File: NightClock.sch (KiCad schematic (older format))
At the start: 11 parts, among them SW1 PUSH+, SW2 PUSHOK, SW3 PUSH-

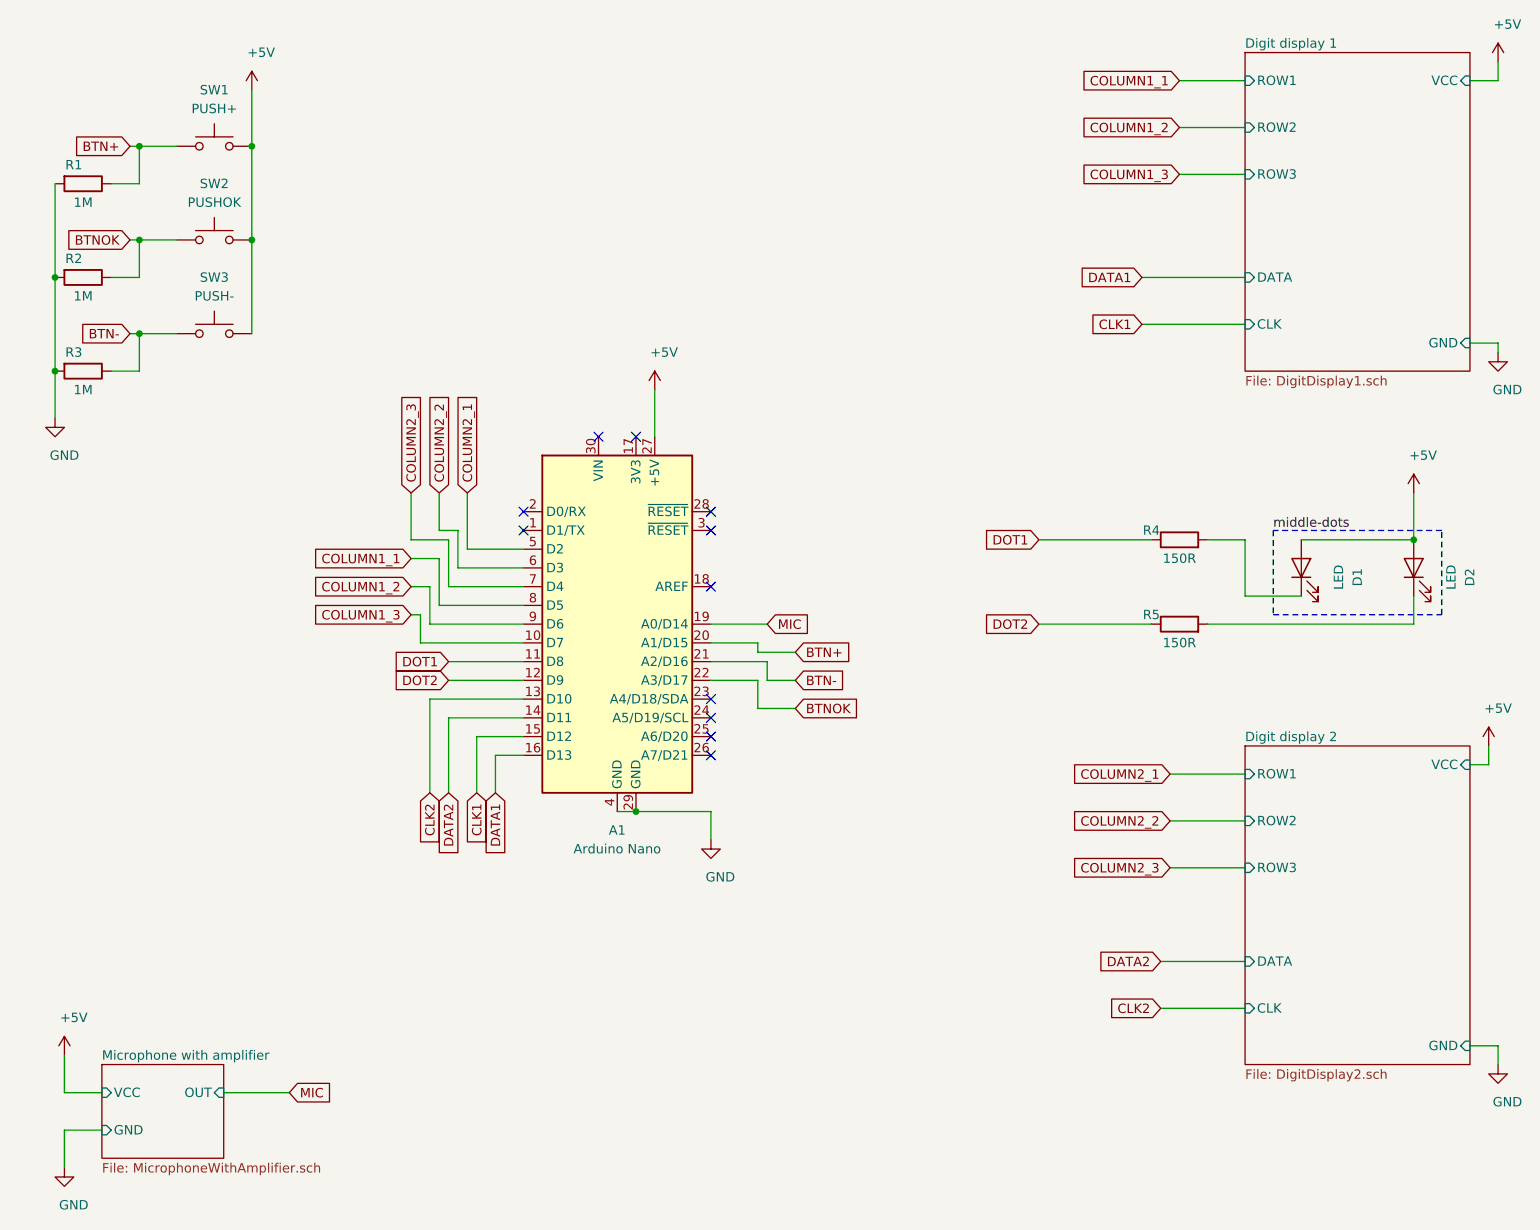
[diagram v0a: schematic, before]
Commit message: add a comparator for setting up an interrupt
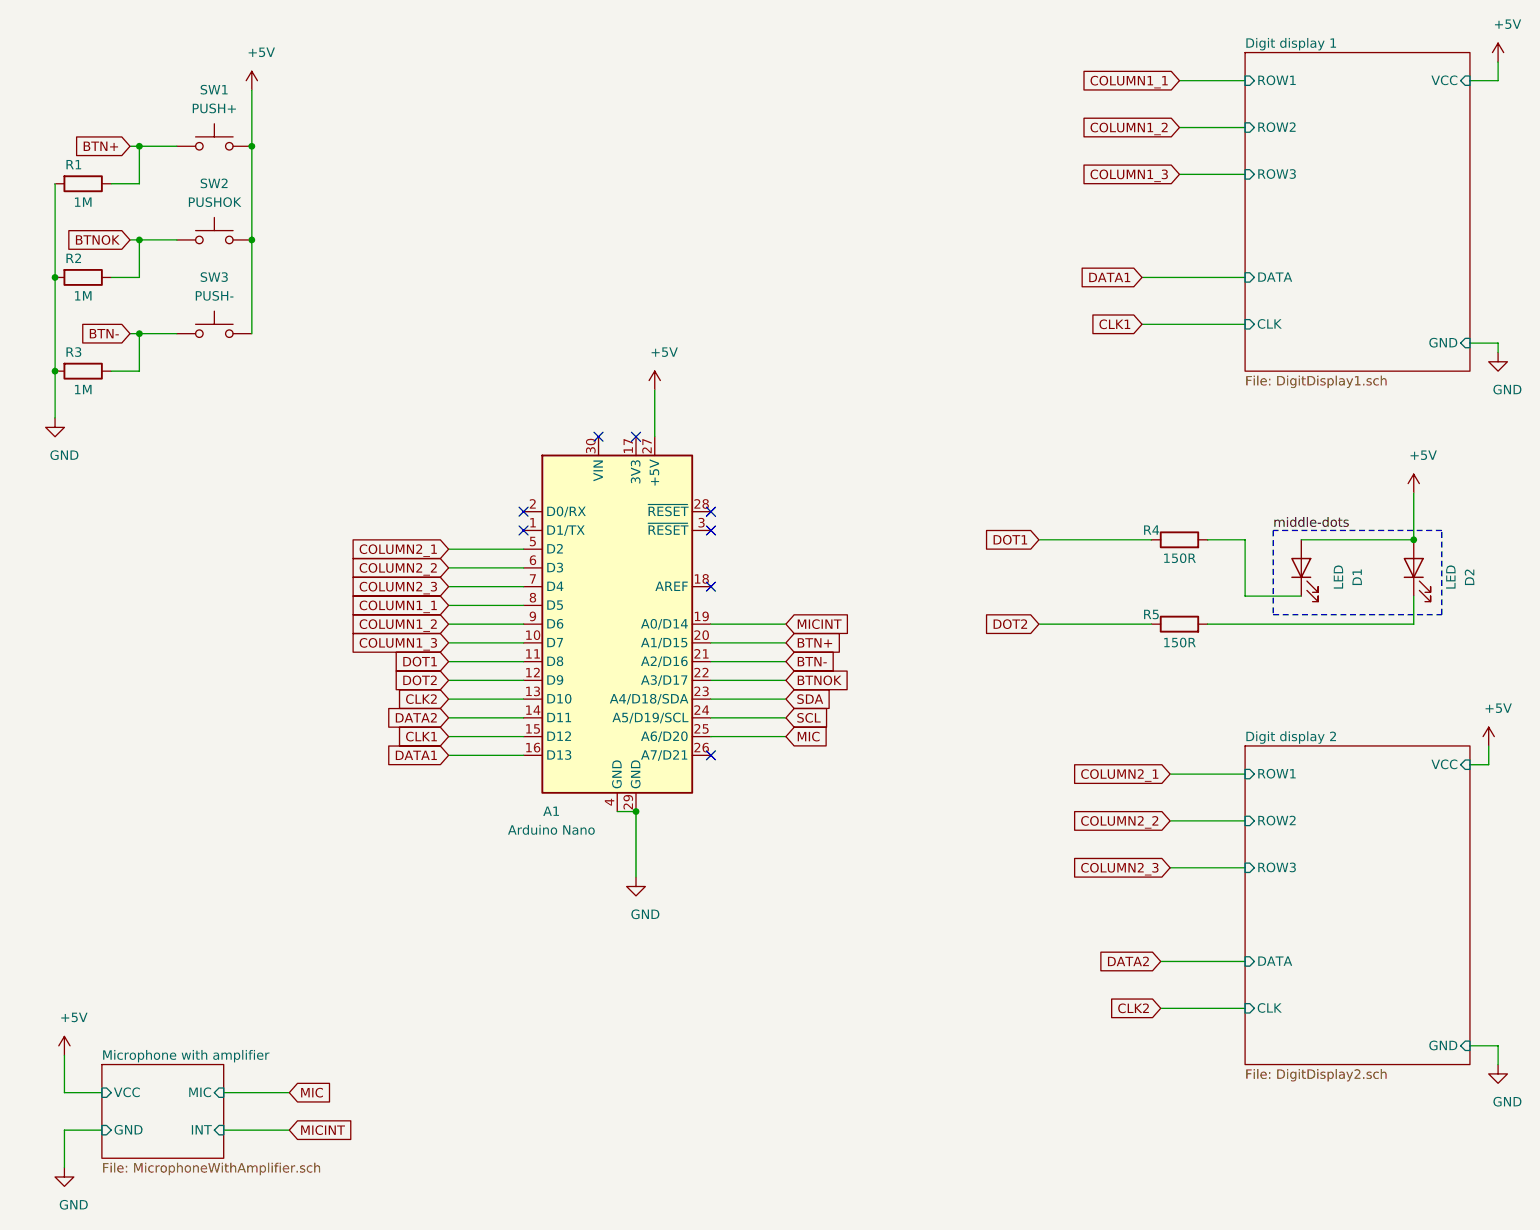
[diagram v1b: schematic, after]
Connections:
- net MIC: now also A1.25 (A6/D20); no longer A1.19 (A0/D14)
- net SDA: now reaches A1.23 (A4/D18/SDA)
- net SCL: now reaches A1.24 (A5/D19/SCL)
- new net MICINT: A1.19 (A0/D14)
- no-connect marks 11 -> 8
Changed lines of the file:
@@
 Sheet 1 4
 Title "Night clock"
-Date "2020-04-10"
+Date "2020-04-11"
 Rev "1"
 Comp "Džejky"
@@
 U 1 1 5E8101CD
 P 4150 3800
-F 0 "A1" H 4150 2700 50  0000 C CNN
-F 1 "Arduino Nano" H 4150 2600 50  0000 C CNN
+F 0 "A1" H 3800 2800 50  0000 C CNN
+F 1 "Arduino Nano" H 3800 2700 50  0000 C CNN
 F 2 "Module:Arduino_Nano" H 4150 3800 50  0001 C CIN
-F 3 "http://www.mouser.com/pdfdocs/Gravitech_Arduino_Nano3_0.pdf" H 4150 3800 50  0001 C CNN
+F 3 "https://content.arduino.cc/assets/Pinout-NANO_latest.pdf" H 4150 3800 50  0001 C CNN
 	1    4150 3800
 	1    0    0    -1
@@
 L power:GND #PWR06
 U 1 1 5E87F331
-P 4650 4950
-F 0 "#PWR06" H 4650 4700 50  0001 C CNN
-F 1 "GND" H 4700 4750 50  0000 C CNN
-F 2 "" H 4650 4950 50  0001 C CNN
-F 3 "" H 4650 4950 50  0001 C CNN
-	1    4650 4950
-	1    0    0    -1
-$EndComp
-Wire Wire Line
-	4650 4950 4650 4800
-Wire Wire Line
-	4650 4800 4250 4800
+P 4250 5150
+F 0 "#PWR06" H 4250 4900 50  0001 C CNN
+F 1 "GND" H 4300 4950 50  0000 C CNN
+F 2 "" H 4250 5150 50  0001 C CNN
+F 3 "" H 4250 5150 50  0001 C CNN
+	1    4250 5150
+	1    0    0    -1
+$EndComp
+Wire Wire Line
+	4250 5150 4250 4800
 Connection ~ 4250 4800
 Wire Wire Line
@@
 Text GLabel 2400 6300 2    50   Input ~ 0
 MIC
-Text GLabel 4950 3800 2    50   Input ~ 0
-MIC
-Wire Wire Line
-	4950 3800 4650 3800
-Text GLabel 5100 3950 2    50   Input ~ 0
+Text GLabel 5050 3900 2    50   Input ~ 0
 BTN+
-Text GLabel 5100 4100 2    50   Input ~ 0
+Text GLabel 5050 4000 2    50   Input ~ 0
 BTN-
-Text GLabel 5100 4250 2    50   Input ~ 0
+Text GLabel 5050 4100 2    50   Input ~ 0
 BTNOK
-Wire Wire Line
-	5100 3950 4900 3950
-Wire Wire Line
-	4900 3950 4900 3900
-Wire Wire Line
-	4900 3900 4650 3900
-Wire Wire Line
-	4650 4000 4950 4000
-Wire Wire Line
-	4950 4000 4950 4100
-Wire Wire Line
-	4950 4100 5100 4100
-Wire Wire Line
-	5100 4250 4900 4250
-Wire Wire Line
-	4900 4250 4900 4100
-Wire Wire Line
-	4900 4100 4650 4100
 Text GLabel 1550 1250 0    50   Input ~ 0
 BTN+
@@
 Text GLabel 7050 5850 0    50   Input ~ 0
 CLK2
-Text GLabel 3500 4700 3    50   Input ~ 0
-DATA1
-Text GLabel 3400 4700 3    50   Input ~ 0
-CLK1
-Text GLabel 3250 4700 3    50   Input ~ 0
+Text GLabel 3250 4300 0    50   Input ~ 0
 DATA2
-Text GLabel 3150 4700 3    50   Input ~ 0
+Text GLabel 3250 4200 0    50   Input ~ 0
 CLK2
-Wire Wire Line
-	3500 4700 3500 4500
-Wire Wire Line
-	3500 4500 3650 4500
-Wire Wire Line
-	3650 4400 3400 4400
-Wire Wire Line
-	3400 4400 3400 4700
-Wire Wire Line
-	3650 4300 3250 4300
-Wire Wire Line
-	3250 4300 3250 4700
-Wire Wire Line
-	3650 4200 3150 4200
-Wire Wire Line
-	3150 4200 3150 4700
 Text GLabel 6400 3350 0    50   Input ~ 0
 DOT1
@@
 Wire Wire Line
 	3650 4100 3250 4100
-Text GLabel 3050 3450 0    50   Input ~ 0
+Text GLabel 3250 3700 0    50   Input ~ 0
 COLUMN1_1
-Text GLabel 3050 3600 0    50   Input ~ 0
+Text GLabel 3250 3800 0    50   Input ~ 0
 COLUMN1_2
-Text GLabel 3050 3750 0    50   Input ~ 0
+Text GLabel 3250 3900 0    50   Input ~ 0
 COLUMN1_3
 Text GLabel 7100 4600 0    50   Input ~ 0
@@
 Text GLabel 7100 5100 0    50   Input ~ 0
 COLUMN2_3
-Text GLabel 3350 3100 1    50   Input ~ 0
+Text GLabel 3250 3400 0    50   Input ~ 0
 COLUMN2_1
-Text GLabel 3200 3100 1    50   Input ~ 0
+Text GLabel 3250 3500 0    50   Input ~ 0
 COLUMN2_2
-Text GLabel 3050 3100 1    50   Input ~ 0
+Text GLabel 3250 3600 0    50   Input ~ 0
 COLUMN2_3
 Wire Wire Line
-	3050 3750 3100 3750
-Wire Wire Line
-	3100 3750 3100 3900
-Wire Wire Line
-	3100 3900 3650 3900
-Wire Wire Line
-	3650 3800 3150 3800
-Wire Wire Line
-	3150 3800 3150 3600
-Wire Wire Line
-	3150 3600 3050 3600
-Wire Wire Line
-	3050 3450 3200 3450
-Wire Wire Line
-	3200 3450 3200 3700
-Wire Wire Line
-	3200 3700 3650 3700
-Wire Wire Line
-	3650 3600 3250 3600
-Wire Wire Line
-	3250 3600 3250 3350
-Wire Wire Line
-	3250 3350 3050 3350
-Wire Wire Line
-	3050 3350 3050 3100
-Wire Wire Line
-	3200 3100 3200 3300
-Wire Wire Line
-	3200 3300 3300 3300
-Wire Wire Line
-	3300 3300 3300 3500
-Wire Wire Line
-	3300 3500 3650 3500
-Wire Wire Line
-	3650 3400 3350 3400
-Wire Wire Line
-	3350 3400 3350 3100
+	3250 3900 3650 3900
+Wire Wire Line
+	3650 3800 3250 3800
 NoConn ~ 4650 4500
-NoConn ~ 4650 4400
-NoConn ~ 4650 4300
-NoConn ~ 4650 4200
 NoConn ~ 4650 3600
 NoConn ~ 4650 3300
@@
 F0 "Microphone with amplifier" 50
 F1 "MicrophoneWithAmplifier.sch" 50
-F2 "OUT" I R 2050 6300 50
+F2 "MIC" I R 2050 6300 50
 F3 "VCC" I L 1400 6300 50
 F4 "GND" I L 1400 6500 50
+F5 "INT" I R 2050 6500 50
 $EndSheet
 Wire Wire Line
@@
 	1    0    0    -1
 $EndComp
+Text GLabel 5050 3800 2    50   Input ~ 0
+MICINT
+Wire Wire Line
+	5050 3800 4650 3800
+Wire Wire Line
+	5050 4400 4650 4400
+Text GLabel 5050 4400 2    50   Input ~ 0
+MIC
+Wire Wire Line
+	4650 3900 5050 3900
+Wire Wire Line
+	4650 4000 5050 4000
+Wire Wire Line
+	4650 4100 5050 4100
+Text GLabel 5050 4200 2    50   Input ~ 0
+SDA
+Text GLabel 5050 4300 2    50   Input ~ 0
+SCL
+Wire Wire Line
+	4650 4200 5050 4200
+Wire Wire Line
+	4650 4300 5050 4300
+Wire Wire Line
+	3250 3700 3650 3700
+Wire Wire Line
+	3650 3600 3250 3600
+Wire Wire Line
+	3250 3400 3650 3400
+Wire Wire Line
+	3250 3500 3650 3500
+Wire Wire Line
+	3250 4300 3650 4300
+Wire Wire Line
+	3250 4200 3650 4200
+Text GLabel 3250 4400 0    50   Input ~ 0
+CLK1
+Text GLabel 3250 4500 0    50   Input ~ 0
+DATA1
+Wire Wire Line
+	3250 4400 3650 4400
+Wire Wire Line
+	3250 4500 3650 4500
+Text GLabel 2400 6500 2    50   Input ~ 0
+MICINT
+Wire Wire Line
+	2400 6500 2050 6500
 $EndSCHEMATC

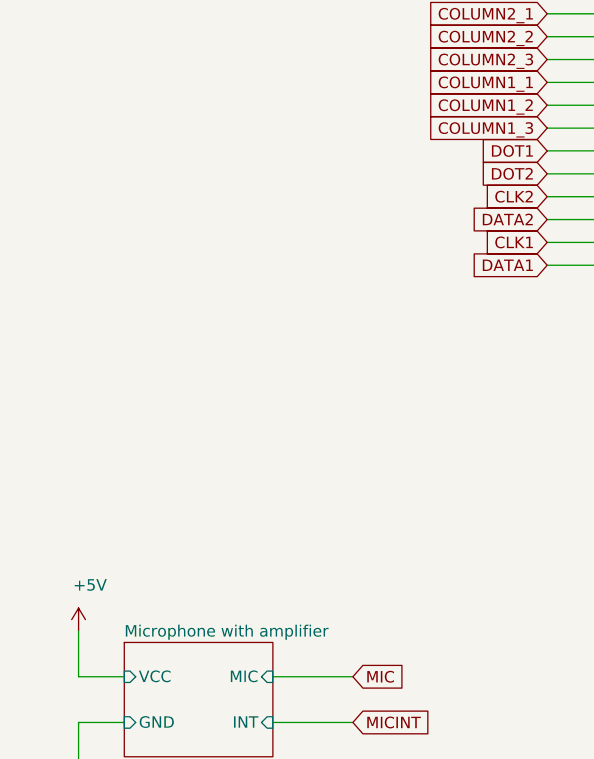
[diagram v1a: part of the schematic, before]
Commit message: add the RTC module and base prototype pcb layout
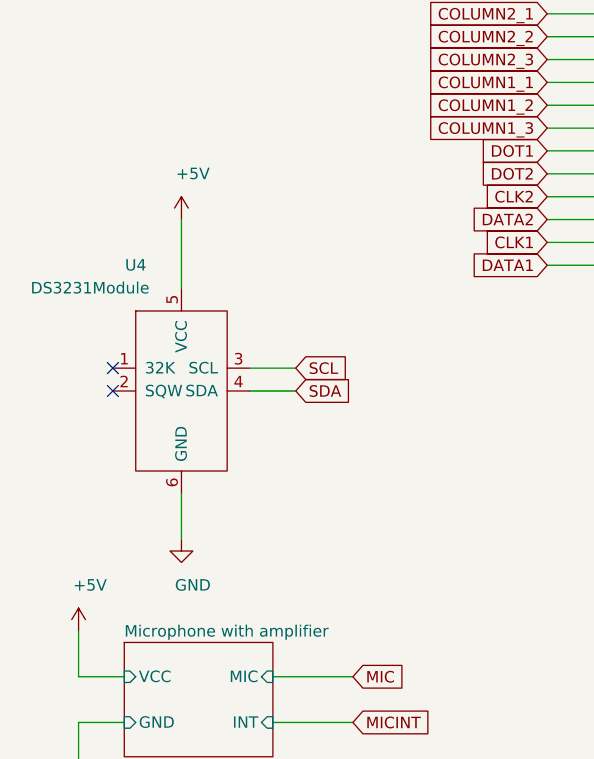
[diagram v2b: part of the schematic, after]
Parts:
- added U4: DS3231Module, Connector_PinSocket_2.54mm:PinSocket_1x06_P2.54mm_Vertical, symbol NightClockSymbols:DS3231Module
- R1, R2, R3: footprint Resistor_THT:R_Axial_DIN0411_L9.9mm_D3.6mm_P15.24mm_Horizontal -> Resistor_THT:R_Axial_DIN0207_L6.3mm_D2.5mm_P7.62mm_Horizontal
- R4, R5: footprint Resistor_SMD:R_0201_0603Metric -> Resistor_SMD:R_0805_2012Metric
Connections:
- net +5V: now also U4.5 (VCC)
- net GND: now also U4.6 (GND)
- net SCL: now also U4.3 (SCL)
- net SDA: now also U4.4 (SDA)
- no-connect marks 8 -> 10
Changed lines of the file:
@@
 F 0 "R4" V 7200 3500 50  0000 C CNN
 F 1 "150R" V 7050 3350 50  0000 C CNN
-F 2 "Resistor_SMD:R_0201_0603Metric" V 7080 3350 50  0001 C CNN
+F 2 "Resistor_SMD:R_0805_2012Metric" V 7080 3350 50  0001 C CNN
 F 3 "~" H 7150 3350 50  0001 C CNN
 	1    7150 3350
@@
 F 0 "R5" V 7200 3950 50  0000 C CNN
 F 1 "150R" V 7050 3800 50  0000 C CNN
-F 2 "Resistor_SMD:R_0201_0603Metric" V 7080 3800 50  0001 C CNN
+F 2 "Resistor_SMD:R_0805_2012Metric" V 7080 3800 50  0001 C CNN
 F 3 "~" H 7150 3800 50  0001 C CNN
 	1    7150 3800
@@
 F 0 "R1" V 1200 1400 50  0000 C CNN
 F 1 "1M" V 1400 1450 50  0000 C CNN
-F 2 "Resistor_THT:R_Axial_DIN0411_L9.9mm_D3.6mm_P15.24mm_Horizontal" V 1230 1450 50  0001 C CNN
+F 2 "Resistor_THT:R_Axial_DIN0207_L6.3mm_D2.5mm_P7.62mm_Horizontal" V 1230 1450 50  0001 C CNN
 F 3 "~" H 1300 1450 50  0001 C CNN
 	1    1300 1450
@@
 F 0 "R2" V 1200 1900 50  0000 C CNN
 F 1 "1M" V 1400 1950 50  0000 C CNN
-F 2 "Resistor_THT:R_Axial_DIN0411_L9.9mm_D3.6mm_P15.24mm_Horizontal" V 1230 1950 50  0001 C CNN
+F 2 "Resistor_THT:R_Axial_DIN0207_L6.3mm_D2.5mm_P7.62mm_Horizontal" V 1230 1950 50  0001 C CNN
 F 3 "~" H 1300 1950 50  0001 C CNN
 	1    1300 1950
@@
 F 0 "R3" V 1200 2400 50  0000 C CNN
 F 1 "1M" V 1400 2450 50  0000 C CNN
-F 2 "Resistor_THT:R_Axial_DIN0411_L9.9mm_D3.6mm_P15.24mm_Horizontal" V 1230 2450 50  0001 C CNN
+F 2 "Resistor_THT:R_Axial_DIN0207_L6.3mm_D2.5mm_P7.62mm_Horizontal" V 1230 2450 50  0001 C CNN
 F 3 "~" H 1300 2450 50  0001 C CNN
 	1    1300 2450
@@
 Wire Wire Line
 	2400 6500 2050 6500
+$Comp
+L NightClockSymbols:DS3231Module U4
+U 1 1 5E9277C8
+P 1650 5050
+F 0 "U4" H 1450 5600 50  0000 C CNN
+F 1 "DS3231Module" H 1250 5500 50  0000 C CNN
+F 2 "Connector_PinSocket_2.54mm:PinSocket_1x06_P2.54mm_Vertical" H 1650 5050 50  0001 C CNN
+F 3 "" H 1650 5050 50  0001 C CNN
+	1    1650 5050
+	1    0    0    -1
+$EndComp
+Text GLabel 2150 5050 2    50   Input ~ 0
+SDA
+Text GLabel 2150 4950 2    50   Input ~ 0
+SCL
+Wire Wire Line
+	2150 4950 1950 4950
+Wire Wire Line
+	1950 5050 2150 5050
+$Comp
+L power:+5V #PWR012
+U 1 1 5E92F9B7
+P 1650 4300
+F 0 "#PWR012" H 1650 4150 50  0001 C CNN
+F 1 "+5V" H 1700 4500 50  0000 C CNN
+F 2 "" H 1650 4300 50  0001 C CNN
+F 3 "" H 1650 4300 50  0001 C CNN
+	1    1650 4300
+	1    0    0    -1
+$EndComp
+Wire Wire Line
+	1650 4300 1650 4600
+$Comp
+L power:GND #PWR013
+U 1 1 5E931FE4
+P 1650 5700
+F 0 "#PWR013" H 1650 5450 50  0001 C CNN
+F 1 "GND" H 1700 5500 50  0000 C CNN
+F 2 "" H 1650 5700 50  0001 C CNN
+F 3 "" H 1650 5700 50  0001 C CNN
+	1    1650 5700
+	1    0    0    -1
+$EndComp
+Wire Wire Line
+	1650 5700 1650 5500
+NoConn ~ 1350 4950
+NoConn ~ 1350 5050
 $EndSCHEMATC

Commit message: make the pcb design
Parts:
- SW1, SW2, SW3: footprint (none) -> NightClockFootprints:PushButtonBlack
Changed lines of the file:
@@
 F 0 "SW1" H 2000 1550 50  0000 C CNN
 F 1 "PUSH+" H 2000 1450 50  0000 C CNN
-F 2 "" H 2000 1450 50  0001 C CNN
+F 2 "NightClockFootprints:PushButtonBlack" H 2000 1450 50  0001 C CNN
 F 3 "~" H 2000 1450 50  0001 C CNN
 	1    2000 1250
@@
 F 0 "SW2" H 2000 2050 50  0000 C CNN
 F 1 "PUSHOK" H 2000 1950 50  0000 C CNN
-F 2 "" H 2000 1950 50  0001 C CNN
+F 2 "NightClockFootprints:PushButtonBlack" H 2000 1950 50  0001 C CNN
 F 3 "~" H 2000 1950 50  0001 C CNN
 	1    2000 1750
@@
 F 0 "SW3" H 2000 2550 50  0000 C CNN
 F 1 "PUSH-" H 2000 2450 50  0000 C CNN
-F 2 "" H 2000 2450 50  0001 C CNN
+F 2 "NightClockFootprints:PushButtonBlack" H 2000 2450 50  0001 C CNN
 F 3 "~" H 2000 2450 50  0001 C CNN
 	1    2000 2250
